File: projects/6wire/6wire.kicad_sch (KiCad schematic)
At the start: 8 parts, among them J1 USB_B_Micro, J2 guard, J3 4wire, U1 AZ1117-3.3

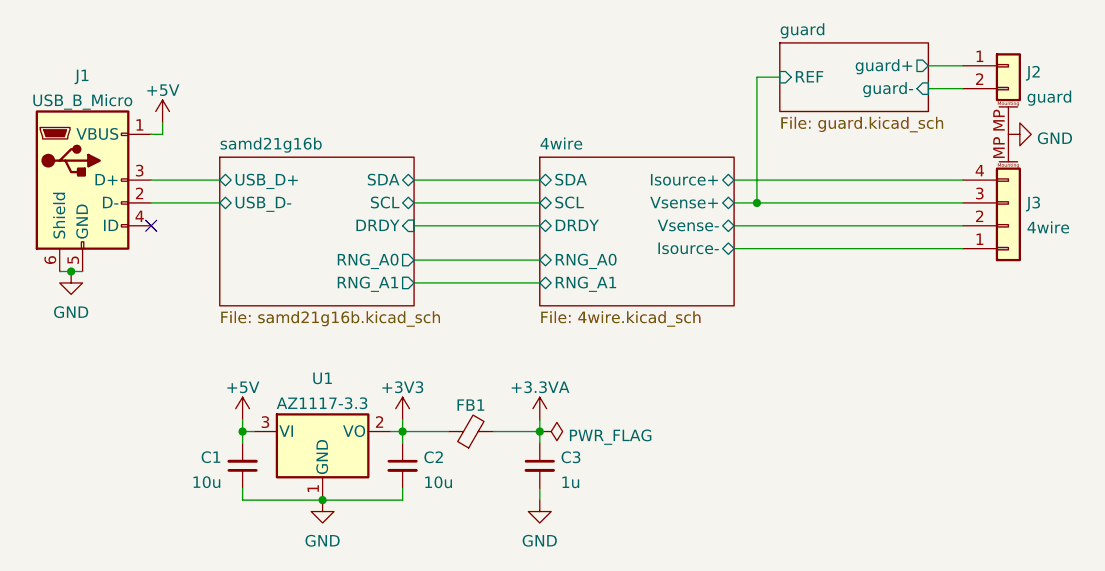
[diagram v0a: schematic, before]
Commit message: update 6wire to v1.1
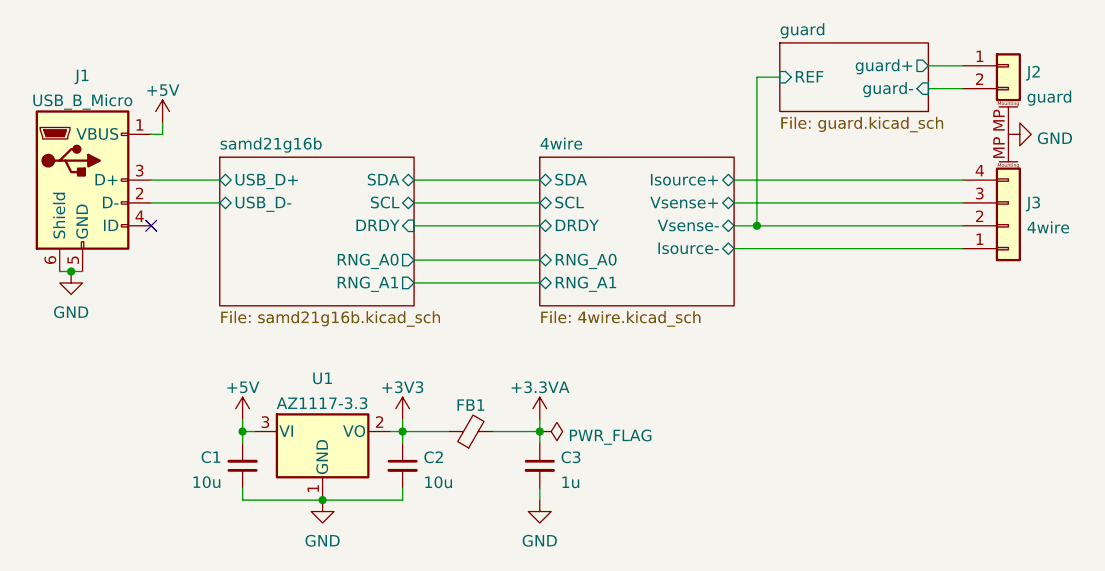
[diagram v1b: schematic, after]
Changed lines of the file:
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@@
 (kicad_sch (version 20211123) (generator eeschema)
   (paper "A4")
-  (junction (at 176.53 96.52) (diameter 0) (color 0 0 0 0)
-  )
   (junction (at 137.16 121.92) (diameter 0) (color 0 0 0 0)
   )
   (junction (at 128.27 129.54) (diameter 0) (color 0 0 0 0)
+  )
+  (junction (at 176.53 99.06) (diameter 0) (color 0 0 0 0)
   )
   (junction (at 100.33 104.14) (diameter 0) (color 0 0 0 0)
@@
   )
   (no_connect (at 109.22 99.06))
+  (wire (pts (xy 176.53 99.06) (xy 173.99 99.06))
+    (stroke (width 0) (type default) (color 0 0 0 0))
+  )
   (wire (pts (xy 99.06 104.14) (xy 100.33 104.14))
     (stroke (width 0) (type default) (color 0 0 0 0))
@@
     (stroke (width 0) (type default) (color 0 0 0 0))
   )
+  (wire (pts (xy 176.53 82.55) (xy 176.53 99.06))
+    (stroke (width 0) (type default) (color 0 0 0 0))
+  )
   (wire (pts (xy 137.16 121.92) (xy 137.16 123.19))
     (stroke (width 0) (type default) (color 0 0 0 0))
@@
     (stroke (width 0) (type default) (color 0 0 0 0))
   )
-  (wire (pts (xy 176.53 96.52) (xy 173.99 96.52))
+  (wire (pts (xy 173.99 96.52) (xy 199.39 96.52))
     (stroke (width 0) (type default) (color 0 0 0 0))
   )
@@
     (stroke (width 0) (type default) (color 0 0 0 0))
   )
-  (wire (pts (xy 199.39 96.52) (xy 176.53 96.52))
-    (stroke (width 0) (type default) (color 0 0 0 0))
-  )
   (wire (pts (xy 179.07 82.55) (xy 176.53 82.55))
     (stroke (width 0) (type default) (color 0 0 0 0))
@@
     (stroke (width 0) (type default) (color 0 0 0 0))
   )
-  (wire (pts (xy 199.39 99.06) (xy 173.99 99.06))
+  (wire (pts (xy 199.39 99.06) (xy 176.53 99.06))
     (stroke (width 0) (type default) (color 0 0 0 0))
   )
@@
     (stroke (width 0) (type default) (color 0 0 0 0))
   )
-  (wire (pts (xy 176.53 82.55) (xy 176.53 96.52))
-    (stroke (width 0) (type default) (color 0 0 0 0))
-  )
